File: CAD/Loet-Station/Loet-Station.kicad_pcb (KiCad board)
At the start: 2 copper layers, 42 parts, among them J101 Weller Tip, J102 Conn_Power, J501 OLED, J601 IO_Conn, Q101 BC547, Q102 IRF9540N, SW101 SW_On, SW102 SW_Down, SW103 SW_Up, SW104 SW_T3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

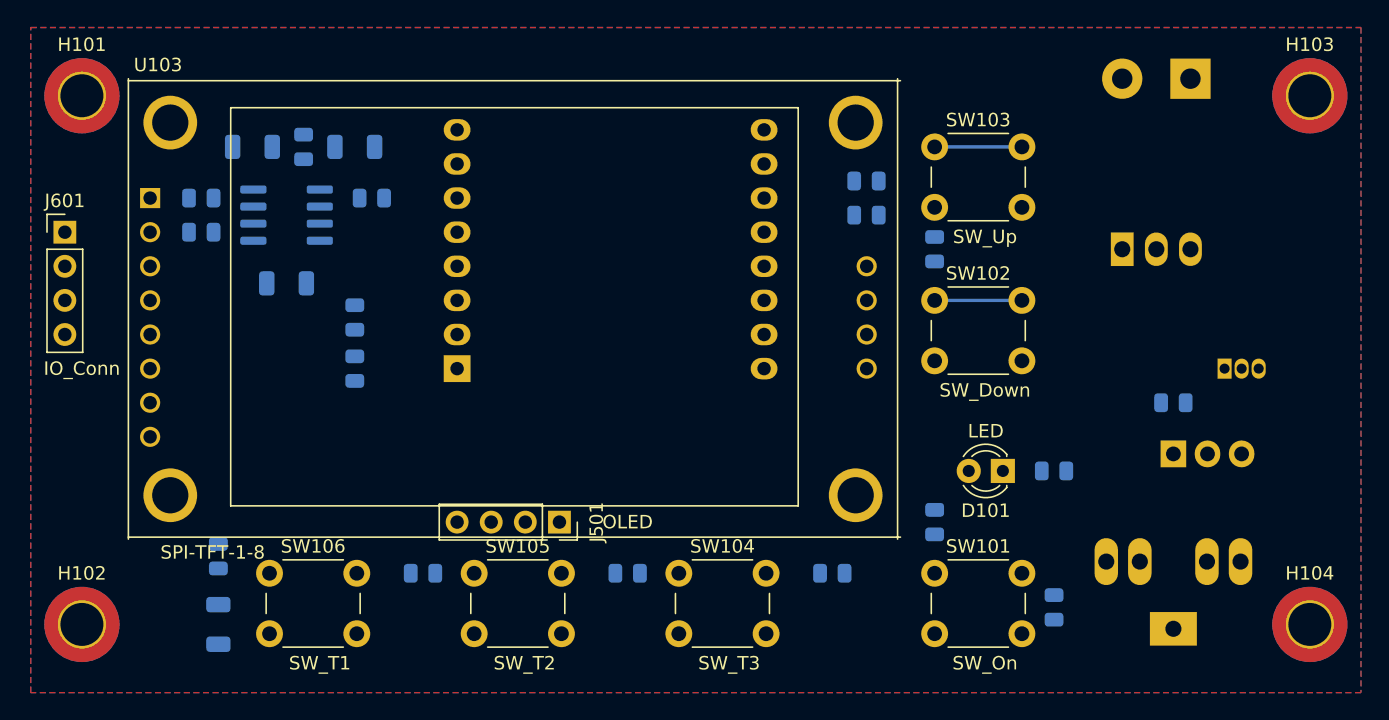
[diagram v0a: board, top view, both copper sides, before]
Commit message: esp32-mini added, pwm driver for 24v
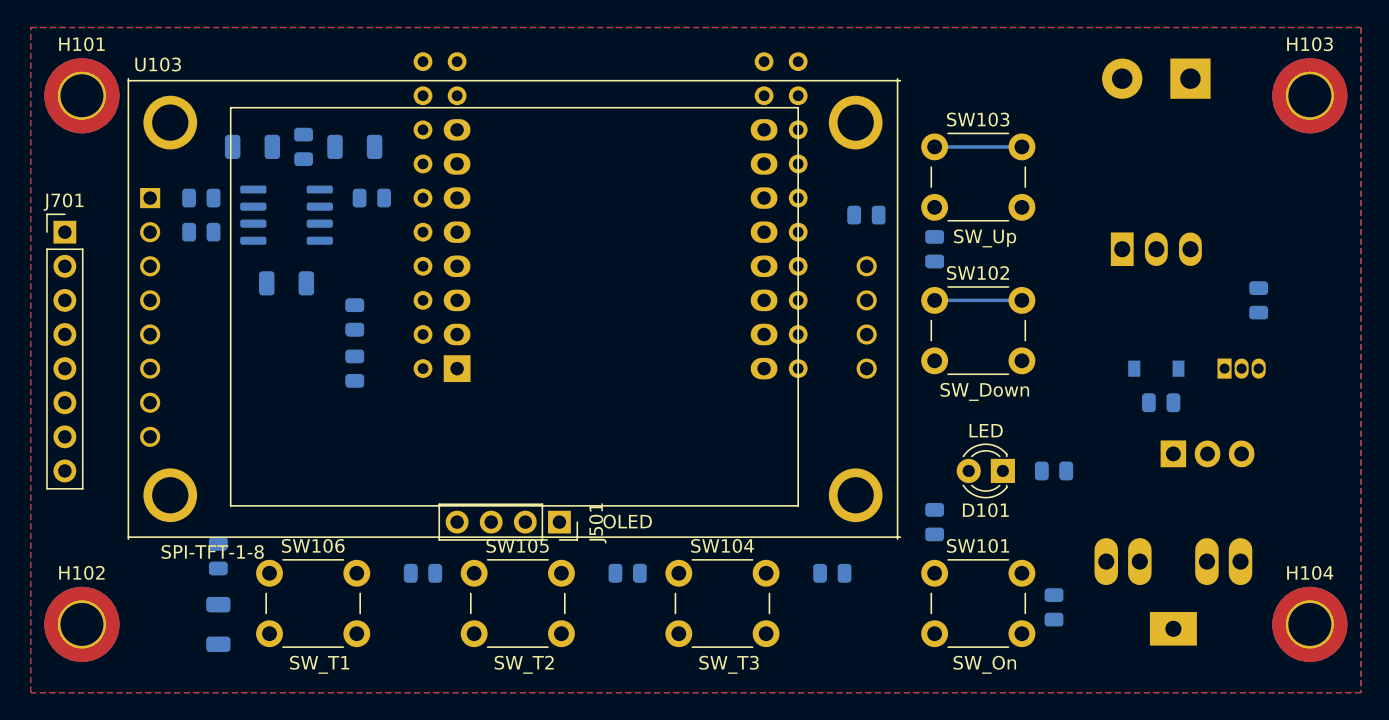
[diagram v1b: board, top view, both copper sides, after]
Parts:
- removed J601: IO_Conn, Connector_PinHeader_2.54mm:PinHeader_1x04_P2.54mm_Vertical
- added D102: D_Zener, Diode_SMD:D_SOD-123, B.Cu at (172.7, 100.3)
- added J701: IO_Conn, Connector_PinHeader_2.54mm:PinHeader_1x08_P2.54mm_Vertical, F.Cu at (91.4, 90.2)
- added U401: mini_esp32, ESP32_mini:ESP32_mini, B.Cu at (132.1, 88.9)
- R102, R107: value R -> 1k
- moved R105 30.5 mm to (180.3, 95.2), turned to 90 degrees
- moved R107 0.91 mm to (173.1, 102.9)
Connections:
- J501 pad 1: VCC -> +3V3
- Q101 pad 3: GND -> Net-(Q101-Pad3)
- R105 pad 1: Net-(Q101-Pad2) -> Net-(Q101-Pad3)

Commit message: changed d1 mini pins, optional i2c oled
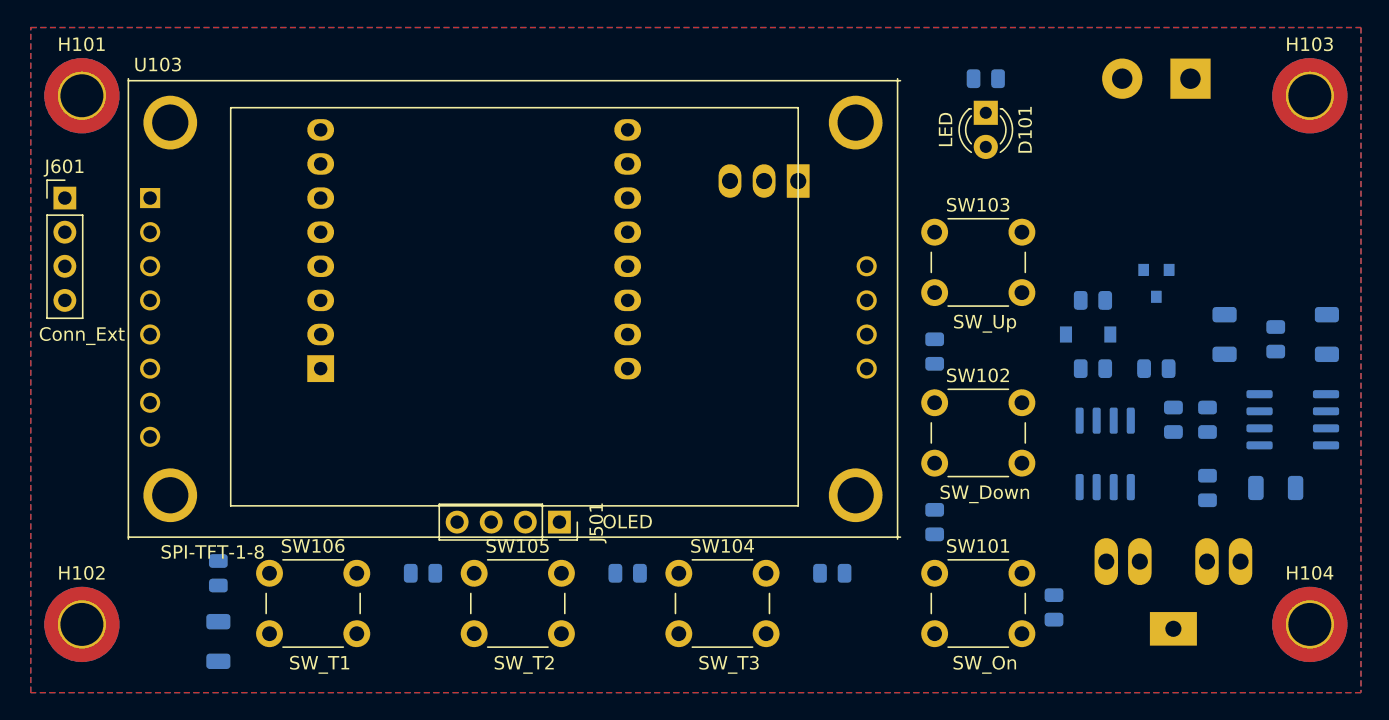
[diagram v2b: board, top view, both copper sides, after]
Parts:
- removed J701: IO_Conn, Connector_PinHeader_2.54mm:PinHeader_1x08_P2.54mm_Vertical
- removed R101: 10k, Resistor_SMD:R_0805_2012Metric
- removed R104: 39k, Resistor_SMD:R_0805_2012Metric
- removed U401: mini_esp32, ESP32_mini:ESP32_mini
- added J601: Conn_Ext, Connector_PinHeader_2.54mm:PinHeader_1x04_P2.54mm_Vertical, F.Cu at (91.4, 87.6)
- Q101: value BC547 -> BC847; footprint Package_TO_SOT_THT:TO-92_Inline -> Package_TO_SOT_SMD:SOT-23
- Q102: value IRF9540N -> IRF7404; footprint Package_TO_SOT_THT:TO-220-3_Vertical -> Package_SO:SOIC-8_3.9x4.9mm_P1.27mm
- moved R103 78.0 mm to (176.5, 109.2), turned to 270 degrees
- moved U101 76.5 mm to (182.9, 104.1)
- moved C103 75.2 mm to (181.6, 109.2)
- moved C101 73.7 mm to (177.8, 97.8), turned to 90 degrees
- moved R106 73.7 mm to (174.0, 104.1), turned to 270 degrees
- moved C102 73.7 mm to (185.4, 97.8), turned to 90 degrees
- moved R108 70.3 mm to (176.5, 104.1)
- moved R109 68.1 mm to (181.6, 98.1), turned to 270 degrees
- moved R110 29.6 mm to (160.0, 78.7)
- moved D101 26.7 mm to (160.0, 81.3), turned to 270 degrees
- moved U102 24.7 mm to (146.1, 86.4), turned to 180 degrees
- moved R102 18.0 mm to (168.0, 95.2), turned to 180 degrees
- moved U301 10.2 mm to (110.5, 100.3)
- moved R105 9.16 mm to (172.7, 100.3), turned to 180 degrees
- moved Q101 8.13 mm to (172.7, 94.0), turned to 270 degrees
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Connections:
- J501 pad 3: I2C_SCL -> DC
- J501 pad 4: I2C_SDA -> CS
- Q101 pad 1: Net-(D102-Pad2) -> Net-(Q101-Pad1)
- Q101 pad 3: Net-(Q101-Pad3) -> Net-(D102-Pad2)
- Q102 pad 1: Net-(D102-Pad2) -> VS
- Q102 pad 2: HEATER -> VS
- R102 pad 1: Net-(Q101-Pad2) -> Net-(Q101-Pad1)
- R105 pad 1: Net-(Q101-Pad3) -> Net-(Q101-Pad2)
- U301 pad 11: PWM -> NEO
- U301 pad 12: NEO -> READ
- U301 pad 13: I2C_SDA -> CS
- U301 pad 14: I2C_SCL -> DC
- U301 pad 2: ADC0 -> TEMP
- U301 pad 3: READ -> Net-(U301-Pad3)
- U301 pad 5: DC -> Net-(U301-Pad5)
- U301 pad 7: CS -> PWM
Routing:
- net Net-(R112-Pad2): track 6.50 -> 0.00 mm
- net Net-(R111-Pad1): track 6.50 -> 0.00 mm

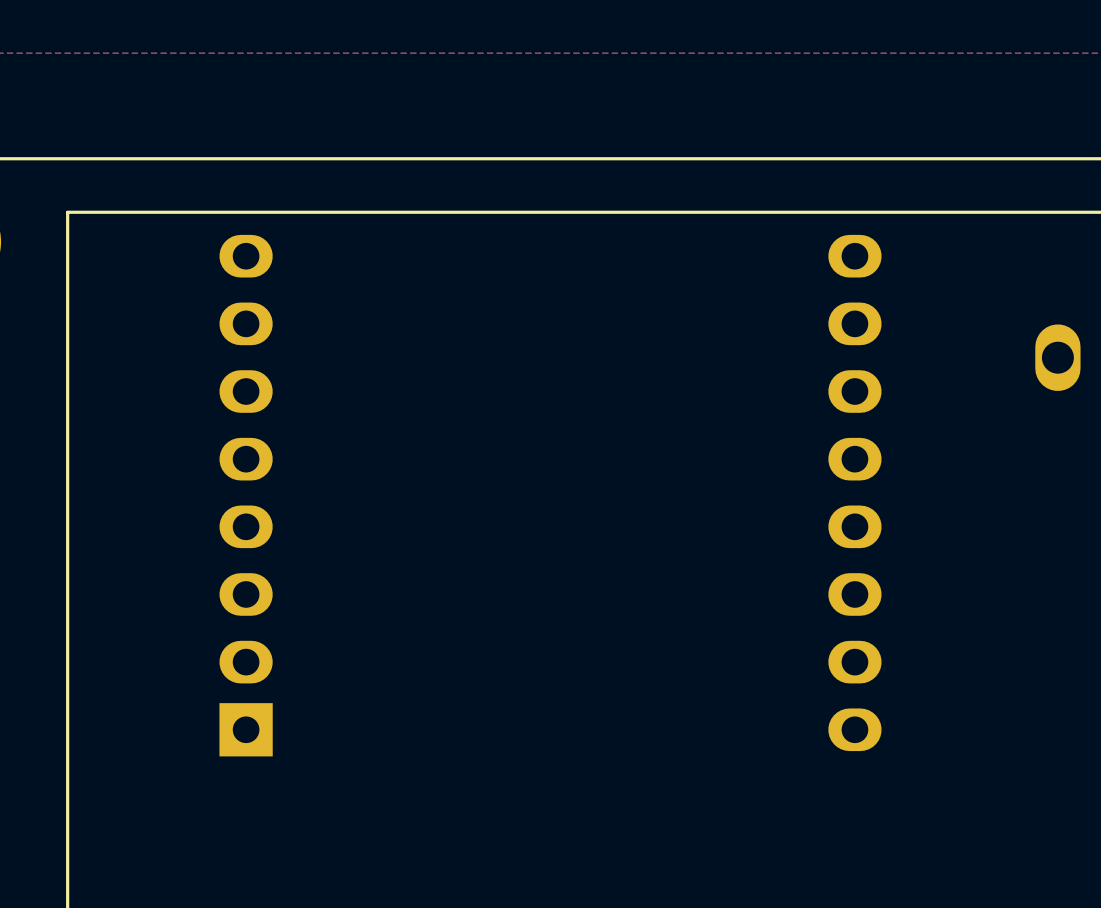
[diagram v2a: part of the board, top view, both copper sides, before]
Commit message: updated schematics
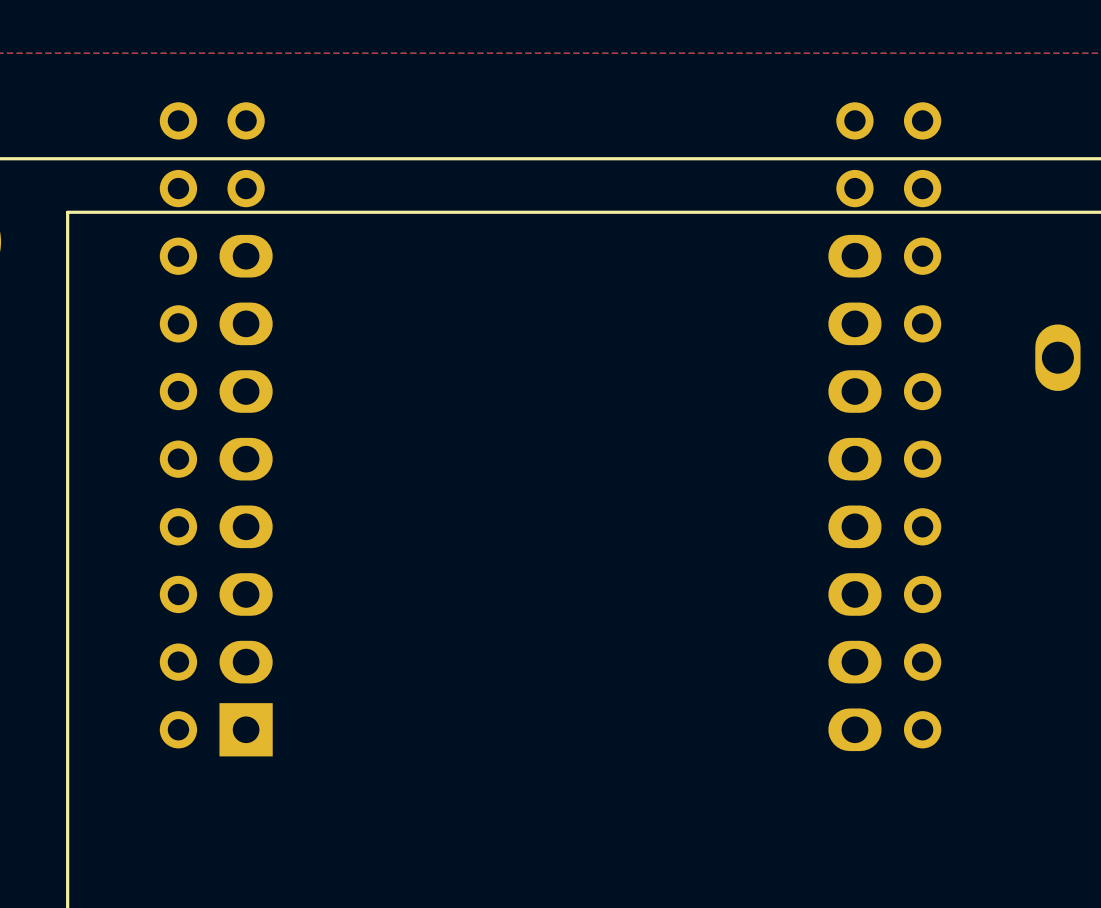
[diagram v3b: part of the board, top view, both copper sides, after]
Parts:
- added U401: mini_esp32, ESP32_mini:ESP32_mini, B.Cu at (121.9, 88.9)

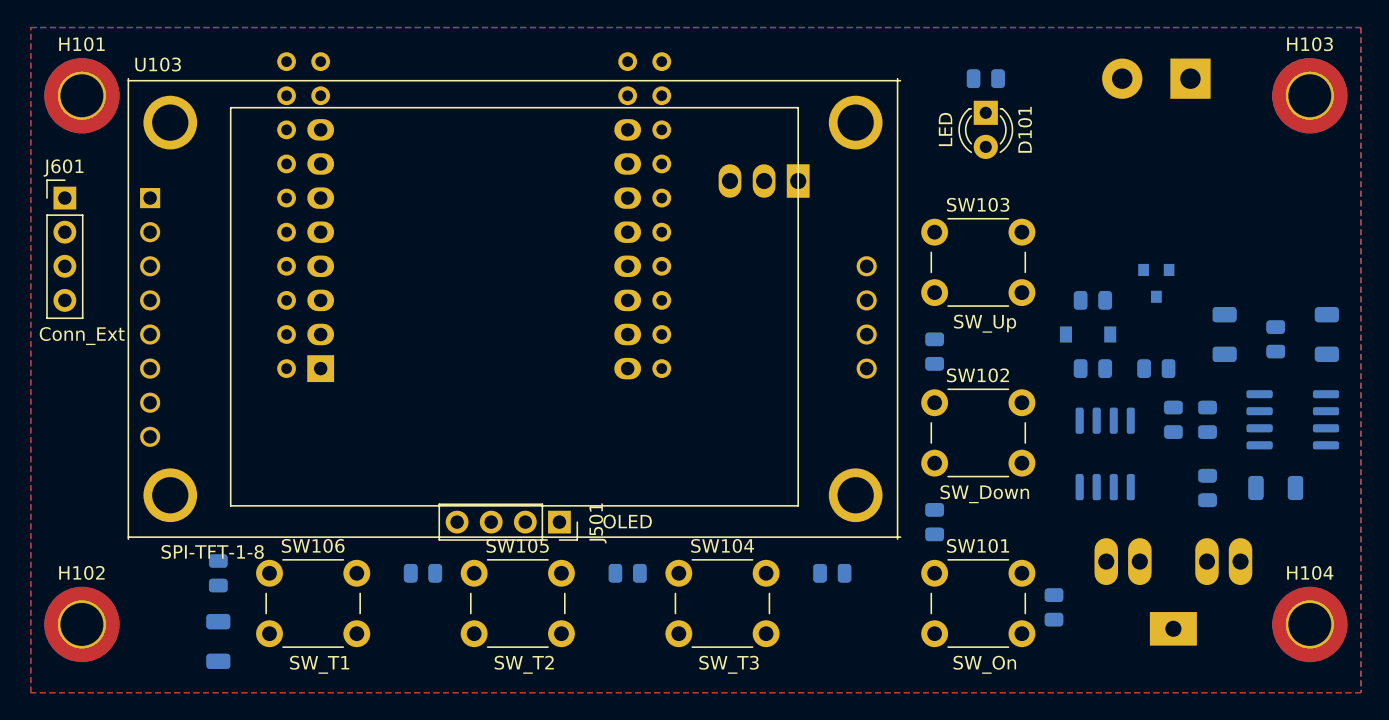
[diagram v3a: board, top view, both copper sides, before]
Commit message: pcb layout loetstation
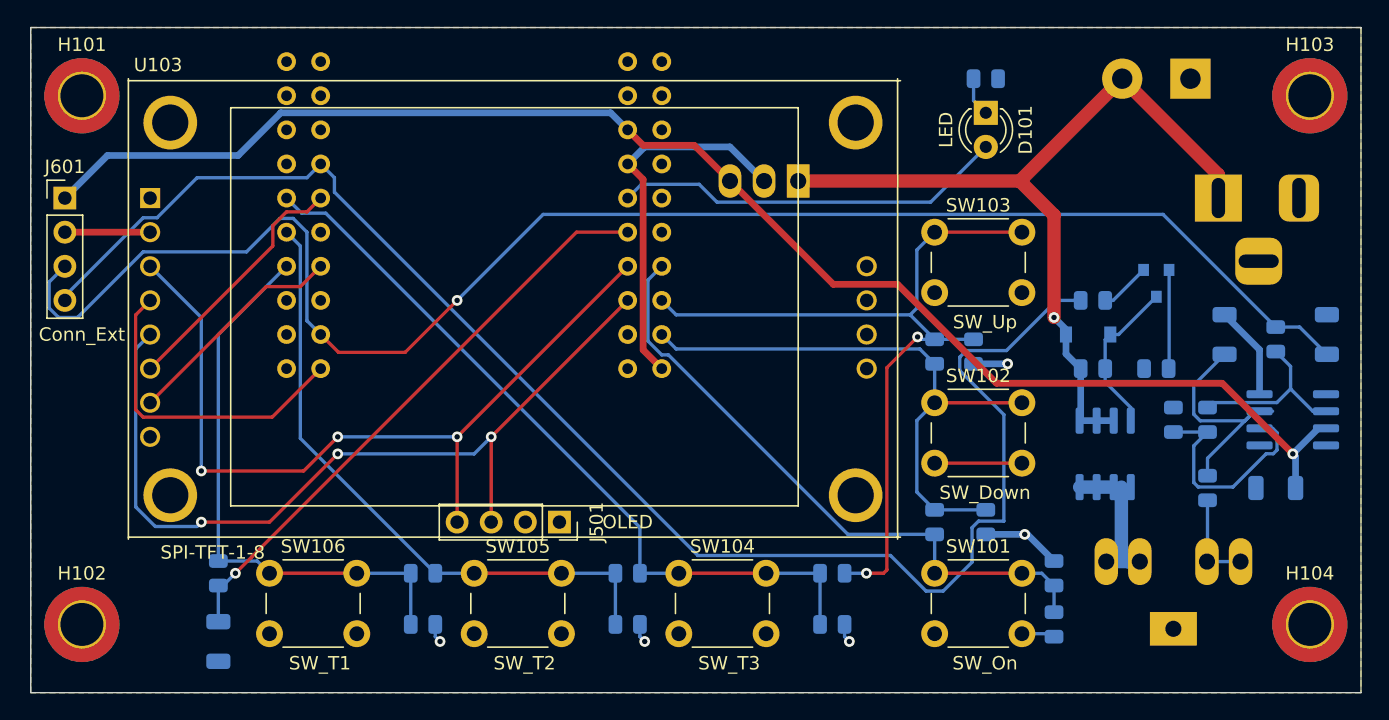
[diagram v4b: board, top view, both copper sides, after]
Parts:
- removed U301: WeMos_D1_mini, Module:WEMOS_D1_mini_light
- added J103: Barrel_Jack_Switch, Connector_BarrelJack:BarrelJack_Horizontal, B.Cu at (177.3, 87.6)
- added R401: R, Resistor_SMD:R_0805_2012Metric, B.Cu at (118.1, 119.4)
- added R402: R, Resistor_SMD:R_0805_2012Metric, B.Cu at (133.3, 119.4)
- added R403: R, Resistor_SMD:R_0805_2012Metric, B.Cu at (148.6, 119.4)
- added R404: R, Resistor_SMD:R_0805_2012Metric, B.Cu at (160.0, 111.8)
- added R405: R, Resistor_SMD:R_0805_2012Metric, B.Cu at (159.1, 99.1)
- added R406: R, Resistor_SMD:R_0805_2012Metric, B.Cu at (165.1, 115.6)
- moved R117 1.27 mm to (165.1, 119.4)
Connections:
- R111 pad 1: Net-(R111-Pad1) -> TDN
- R111 pad 2: Net-(R111-Pad2) -> TON
- R112 pad 1: Net-(R111-Pad1) -> TDN
- R112 pad 2: Net-(R112-Pad2) -> TUP
- R113 pad 1: Net-(R112-Pad2) -> TUP
- R113 pad 2: Net-(R113-Pad2) -> T3
- R114 pad 1: Net-(R113-Pad2) -> T3
- R114 pad 2: Net-(R114-Pad2) -> T2
- R115 pad 1: Net-(R114-Pad2) -> T2
- R115 pad 2: Net-(R115-Pad2) -> T1
- R116 pad 1: Net-(R115-Pad2) -> T1
- R117 pad 1: Net-(R111-Pad2) -> TON
- SW101 pad 1: Net-(R111-Pad2) -> TON
- SW102 pad 1: Net-(R111-Pad1) -> TDN
- SW103 pad 1: Net-(R112-Pad2) -> TUP
- SW104 pad 1: Net-(R113-Pad2) -> T3
- SW105 pad 1: Net-(R114-Pad2) -> T2
- SW106 pad 1: Net-(R115-Pad2) -> T1
- U401 pad 11: Net-(U401-Pad11) -> T3
- U401 pad 2: Net-(U401-Pad2) -> RESET
- U401 pad 24: Net-(U401-Pad24) -> TDN
- U401 pad 26: Net-(U401-Pad26) -> TUP
- U401 pad 28: Net-(U401-Pad28) -> TON
- U401 pad 7: Net-(U401-Pad7) -> T1
- U401 pad 9: Net-(U401-Pad9) -> T2
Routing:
- net TEMP: track 0.00 -> 118.7 mm, vias 0 -> 1
- net PWM: track 0.00 -> 116.6 mm
- net +5V: track 0.00 -> 110.5 mm, vias 0 -> 1
- net DC: track 0.00 -> 63.8 mm, vias 0 -> 3
- net VS: track 0.00 -> 61.4 mm, vias 0 -> 1
- net CS: track 0.00 -> 61.2 mm, vias 0 -> 3
- net TUP: track 0.00 -> 61.1 mm, vias 0 -> 2
- net T3: track 0.00 -> 57.1 mm
- net GND: track 0.00 -> 51.1 mm
- net TON: track 0.00 -> 47.5 mm
- net T2: track 0.00 -> 47.2 mm
- net READ: track 0.00 -> 44.1 mm, vias 0 -> 1
- net TDN: track 0.00 -> 43.5 mm
- net T1: track 0.00 -> 42.6 mm
- net NEO: track 0.00 -> 29.3 mm
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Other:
- board outline added: 99.1 x 49.5 mm

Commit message: Loet-Station v1
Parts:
- removed J601: Conn_Ext, Connector_PinHeader_2.54mm:PinHeader_1x04_P2.54mm_Vertical
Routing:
- net +5V: track 110.5 -> 65.4 mm
- net TEMP: track 118.7 -> 84.0 mm
- net PWM: track 116.6 -> 93.2 mm
- net GND: track 51.1 -> 44.7 mm
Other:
- board text added: "(c) RobotFreak"
- board text added: "+"
- board text added: "-"
- board text added: "16"
- board text added: "18"
- board text added: "21"
- board text added: "22"
- board text added: "23"
- board text added: "25"
- board text added: "27"
- board text added: "32"
- board text added: "33"
- board text added: "34"
- board text added: "35"
- board text added: "36"
- board text added: "5"
- board text added: "C"
- board text added: "CS"
- board text added: "D"
- board text added: "DC"
- board text added: "ESP D1 Mini / ESP32 D1 Mini"
- board text added: "ESP Lötstation v1"
- board text added: "LED"
- board text added: "MOSI"
- board text added: "Res"
- board text added: "SCK"
